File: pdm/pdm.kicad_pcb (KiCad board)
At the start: 2 copper layers, 169.5 x 69 mm, 112 parts, among them J1 Conn_01x04_Male, J2 Conn_01x08_Male, Q1 MMBT3904, Q10 Q_NPN_BCE, Q2 Q_NPN_BCE, Q3 MMBT3904, Q4 Q_NPN_BCE, Q5 MMBT3904, Q6 Q_NPN_BCE, Q7 MMBT3904, Q8 Q_NPN_BCE, Q9 MMBT3904, SW1 SW_Push, U1 AZ1117CH-3_3TRG1, U2 SN65HVD233, U3 STM32F042G6Ux, U4 BTS443P, U5 BTS443P, U6 BTS443P, U7 BTS443P, U8 BTS443P

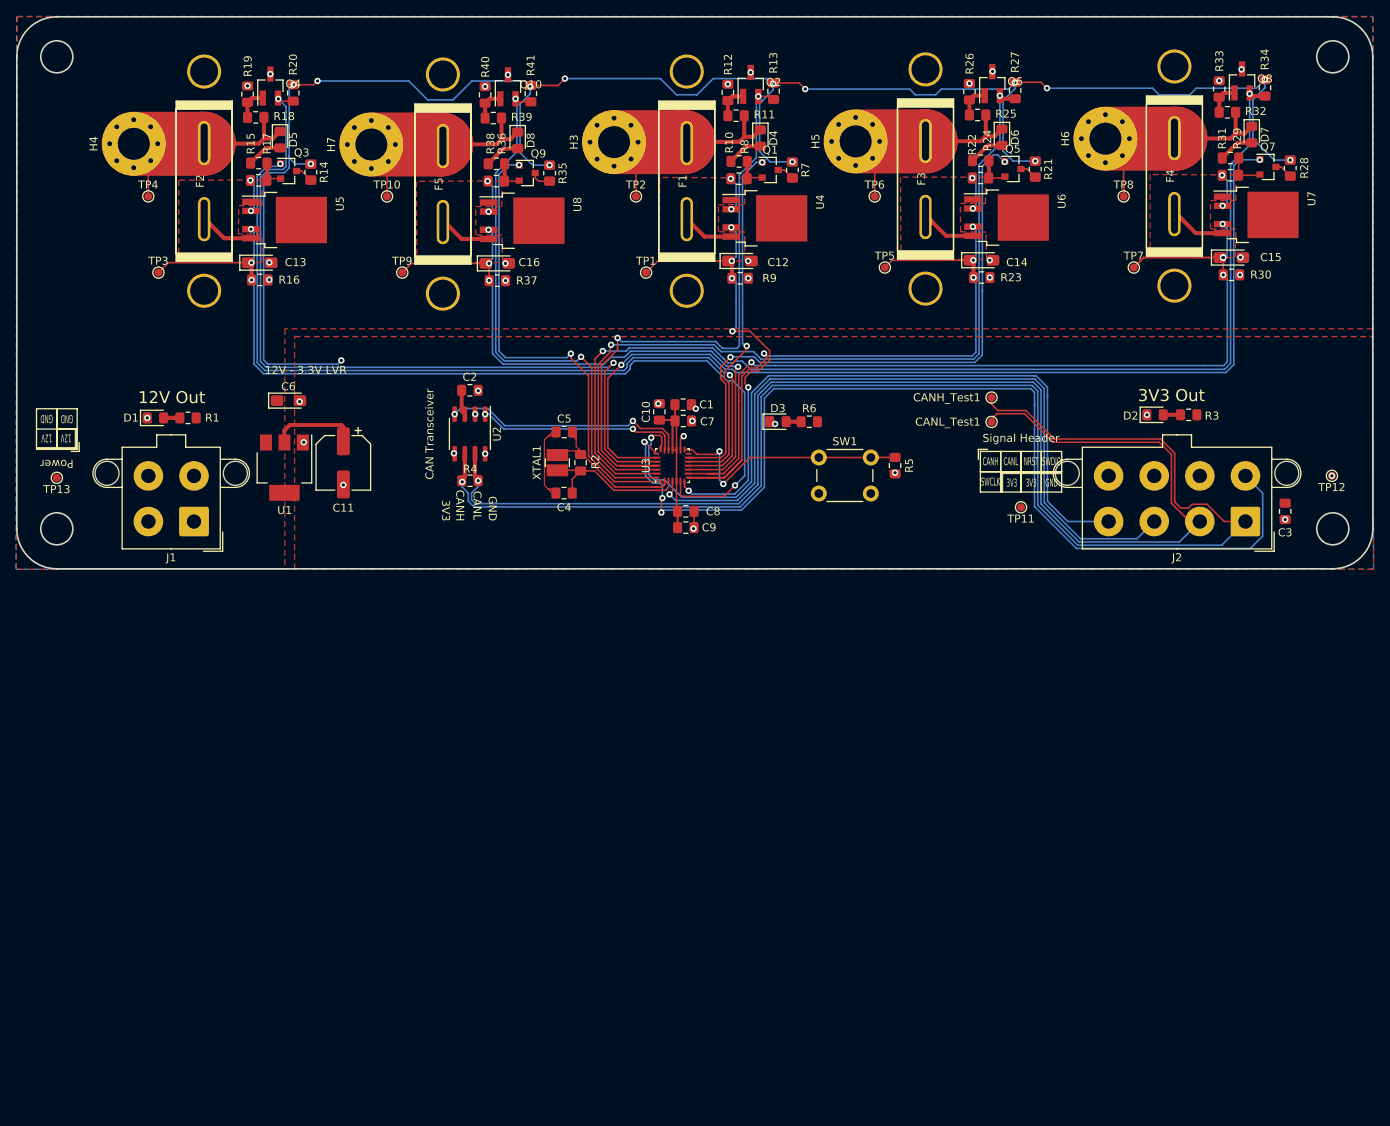
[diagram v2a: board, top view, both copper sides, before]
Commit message: changed layout with two plugs
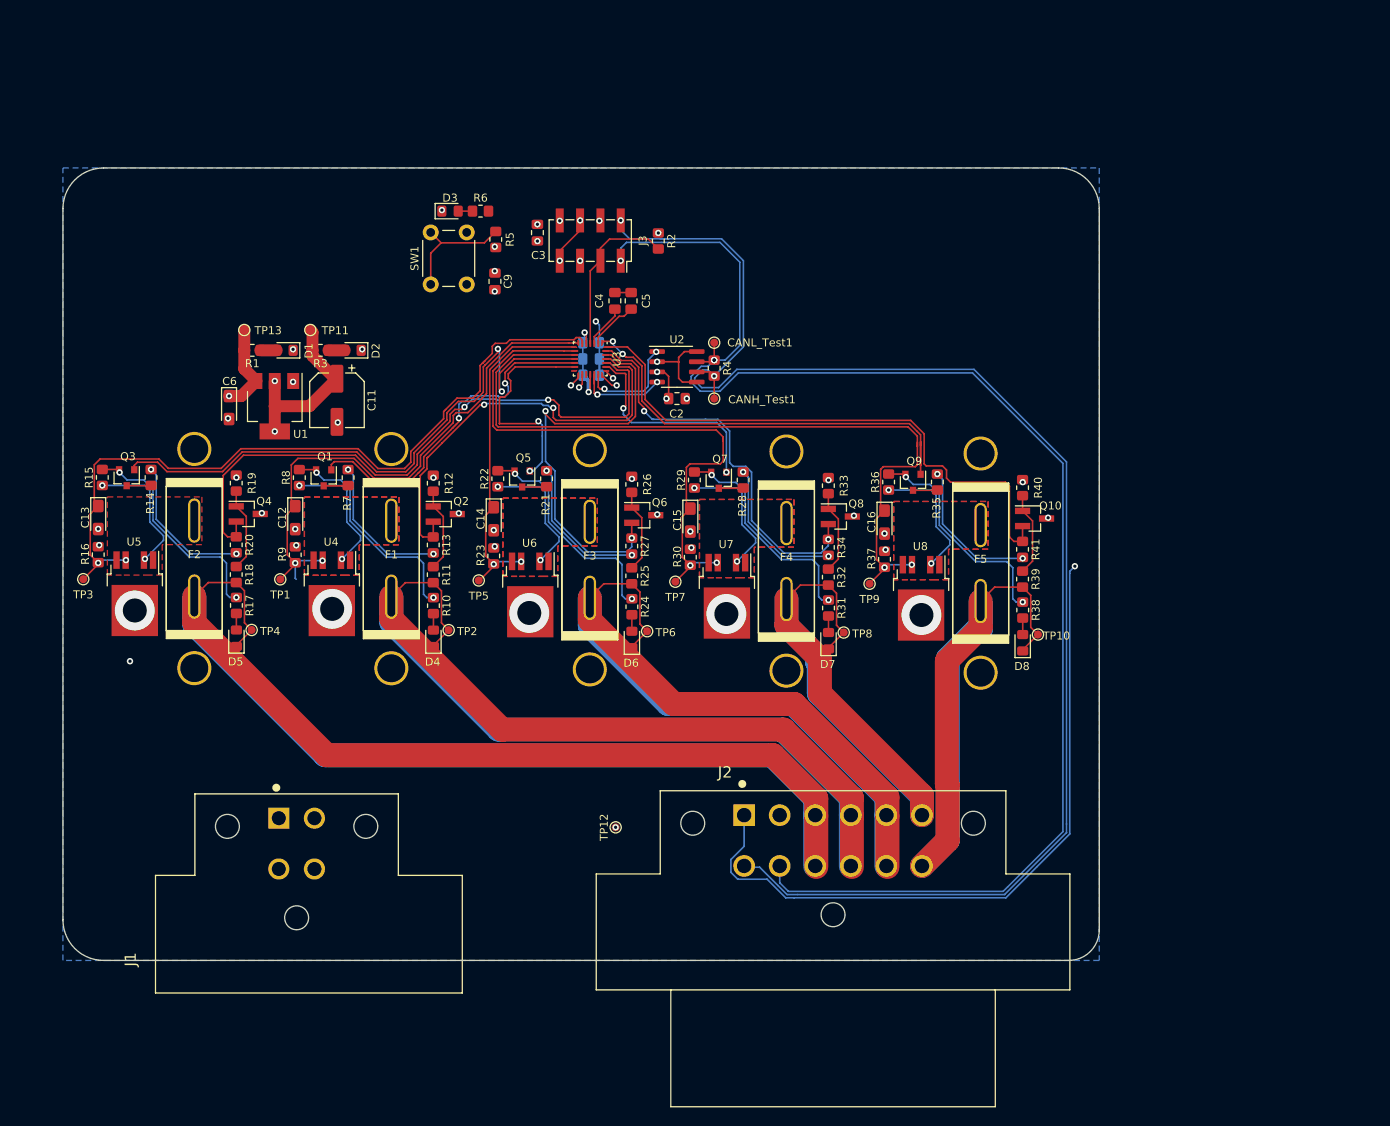
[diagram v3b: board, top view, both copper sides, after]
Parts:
- removed C1: 0.1uF, Capacitor_SMD:C_0805_2012Metric_Pad1.15x1.40mm_HandSolder
- removed H3, H4, H5, H6, H7: MountingHole_Pad, MountingHole:MountingHole_4mm_Pad_Via
- removed XTAL1: NX3225GD-8MHZ-STD-CRA-3, digikey-footprints:SMD-2_3.2x2.5mm
- added J3: Conn_01x08_Male, Connector_PinSocket_2.54mm:PinSocket_2x04_P2.54mm_Vertical_SMD, F.Cu at (170.2, 50.0)
- C10, C7, C8: footprint Capacitor_SMD:C_0805_2012Metric_Pad1.15x1.40mm_HandSolder -> Capacitor_SMD:C_0805_2012Metric_Pad1.18x1.45mm_HandSolder; moved to B.Cu
- C2, C3, C4, C5, C9: footprint Capacitor_SMD:C_0805_2012Metric_Pad1.15x1.40mm_HandSolder -> Capacitor_SMD:C_0805_2012Metric_Pad1.18x1.45mm_HandSolder
- F1, F2, F3, F4, F5: footprint Fuse:blade_fuse_panelized -> pdm_v2:fuseHolder
- J1: footprint Connector_Molex:Molex_Mega-Fit_76829-0004_2x02_P5.70mm_Vertical -> DT13-4P:TE_DT13-4P
- J2: value Conn_01x08_Male -> Conn_01x12_Male; footprint Connector_Molex:Molex_Mega-Fit_76829-0008_2x04_P5.70mm_Vertical -> DT13-12PB-B016:TE_DT13-12PB-B016
- R1, R10, R11, R12, R13, R15, R16, R17, R18, R19, R20, R22, R23, R24, R25, R26, R27, R29, R3, R30, R31, R32, R33, R34, R36, R37, R38, R39, R4, R40, R41, R5, R6, R8, R9: footprint Resistor_SMD:R_0805_2012Metric_Pad1.15x1.40mm_HandSolder -> Resistor_SMD:R_0805_2012Metric_Pad1.20x1.40mm_HandSolder
- R2: value 1M -> 10K; footprint Resistor_SMD:R_0805_2012Metric_Pad1.15x1.40mm_HandSolder -> Resistor_SMD:R_0805_2012Metric_Pad1.20x1.40mm_HandSolder
- moved R3 108.8 mm to (136.5, 63.7), turned to 180 degrees
- moved D2 100.6 mm to (140.5, 63.7), turned to 180 degrees
- moved C3 99.8 mm to (163.6, 49.0), turned to 90 degrees
- moved TP12 99.7 mm to (173.4, 123.3), turned to 90 degrees
- moved TP10 98.1 mm to (226.1, 99.2), turned to 180 degrees
- moved TP11 91.6 mm to (135.2, 61.2), turned to 270 degrees
- moved D8 89.0 mm to (224.2, 100.2), turned to 90 degrees
- moved R39 87.7 mm to (224.2, 92.3), turned to 270 degrees
- moved R38 86.3 mm to (224.2, 96.2), turned to 270 degrees
- moved Q10 85.1 mm to (225.7, 84.7), turned to 0 degrees
- moved R41 83.8 mm to (224.2, 88.6), turned to 270 degrees
- moved R40 83.2 mm to (224.2, 80.9)
- moved D7 82.5 mm to (200.0, 100.0), turned to 90 degrees
- moved F5 82.2 mm to (219.0, 90.3), turned to 180 degrees
- moved U7 81.6 mm to (187.3, 94.4), turned to 270 degrees
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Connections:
- net /fuse_block/vout renamed /fuse_block/out
- net /sheet5F955EDF/vout renamed /sheet5F955EDF/out
- net /sheet5F955F69/vout renamed /sheet5F955F69/out
- net /sheet5F95602F/vout renamed /sheet5F95602F/out
- net /sheet5F9560CD/vout renamed /sheet5F9560CD/out
- D4 pad 1: /sheet5F955EDF/vload -> /vout2
- D5 pad 1: /fuse_block/vload -> /vout1
- D6 pad 1: /sheet5F955F69/vload -> /vout3
- D7 pad 1: /sheet5F95602F/vload -> /vout4
- D8 pad 1: /sheet5F9560CD/vload -> /vout5
- F1 pad 1: /sheet5F955EDF/vload -> /vout2
- F2 pad 1: /fuse_block/vload -> /vout1
- F3 pad 1: /sheet5F955F69/vload -> /vout3
- F4 pad 1: /sheet5F95602F/vload -> /vout4
- F5 pad 1: /sheet5F9560CD/vload -> /vout5
- J1 pad 1: +12V -> GND
- J1 pad 3: GND -> +12V
- J1 pad 4: GND -> +12V
- J2 pad 1: /_P -> +3V3
- J2 pad 2: /_N -> GND
- J2 pad 3: /NRST -> /vout1
- J2 pad 4: /SWDIO -> /vout2
- J2 pad 5: /SWCLK -> /vout3
- J2 pad 6: +3V3 -> /vout4
- J2 pad 7: +3V3 -> /vout5
- J2 pad 8: GND -> /vout3
- R11 pad 2: /sheet5F955EDF/vload -> /vout2
- R18 pad 2: /fuse_block/vload -> /vout1
- R2 pad 1: /OSC_P -> GND
- R2 pad 2: /OSC_N -> /NRST
- R25 pad 2: /sheet5F955F69/vload -> /vout3
- R32 pad 2: /sheet5F95602F/vload -> /vout4
- R39 pad 2: /sheet5F9560CD/vload -> /vout5
- TP10 pad 1: /sheet5F9560CD/vload -> /vout5
- TP2 pad 1: /sheet5F955EDF/vload -> /vout2
- TP4 pad 1: /fuse_block/vload -> /vout1
- TP6 pad 1: /sheet5F955F69/vload -> /vout3
- TP8 pad 1: /sheet5F95602F/vload -> /vout4
- U1 pad 4: (no net) -> +3V3
- U3 pad 17: +3V3 -> (no net)
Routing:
- net /vout1: track 0.00 -> 311.6 mm
- net /vout2: track 0.00 -> 250.6 mm
- net /vout3: track 0.00 -> 189.4 mm
- net /vout5: track 0.00 -> 124.5 mm
- net /vout4: track 0.00 -> 117.8 mm
- net /SWCLK: track 127.0 -> 18.5 mm, vias 3 -> 2
- net /act4: track 124.8 -> 26.8 mm
- net /fuse4: track 138.5 -> 50.3 mm
- net /NRST: track 93.0 -> 20.7 mm, vias 1 -> 0
- net /SWDIO: track 95.6 -> 24.5 mm, vias 1 -> 2
- net +12V: track 0.00 -> 57.6 mm, vias 0 -> 7
- net /fuse3: track 104.7 -> 51.7 mm
- net /act3: track 78.5 -> 28.2 mm
- net +3V3: track 270.4 -> 226.4 mm, vias 15 -> 21
- net /sense3: track 84.7 -> 43.5 mm, vias 4 -> 2
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- added copper zone on In2.Cu, net +12V
- added copper zone on In1.Cu, net +3V3
- removed copper zone on F.Cu, net +12V
- removed copper zone on F.Cu, net +3V3
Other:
- board size 169.5 x 69 mm -> 129.5 x 99.1 mm
- copper layers 2 -> 4
- board text removed: "12V"
- board text removed: "12V - 3.3V LVR"
- board text removed: "12V Out"
- board text removed: "3V3"
- board text removed: "3V3 Out"
- board text removed: "CAN Transceiver"
- board text removed: "CANH"
- board text removed: "CANL"
- board text removed: "GND"
- board text removed: "NRST"
- board text removed: "Power"
- board text removed: "SWCLK"
- board text removed: "SWDIO"
- board text removed: "Signal Header"

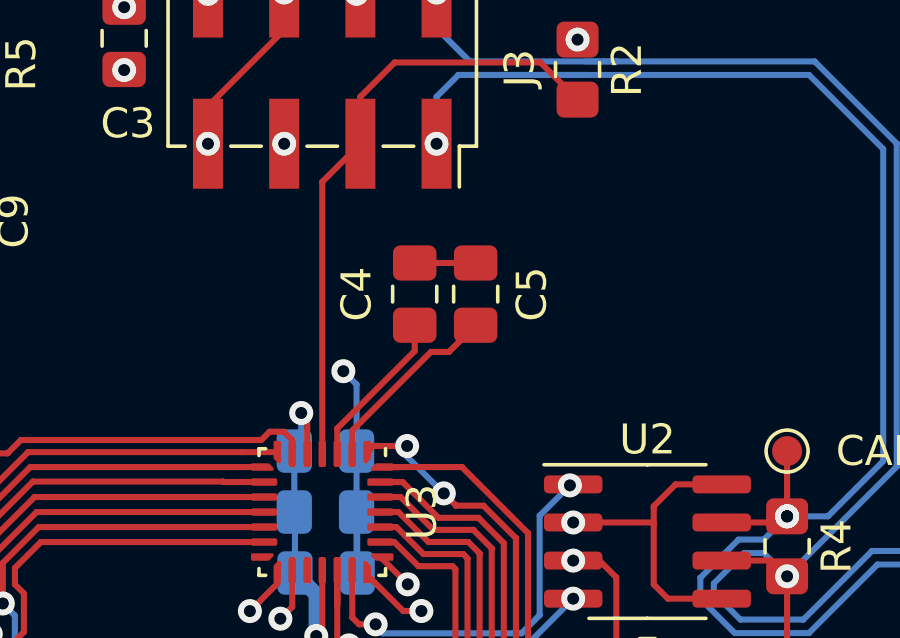
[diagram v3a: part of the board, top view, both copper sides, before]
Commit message: added placeholder oscillator
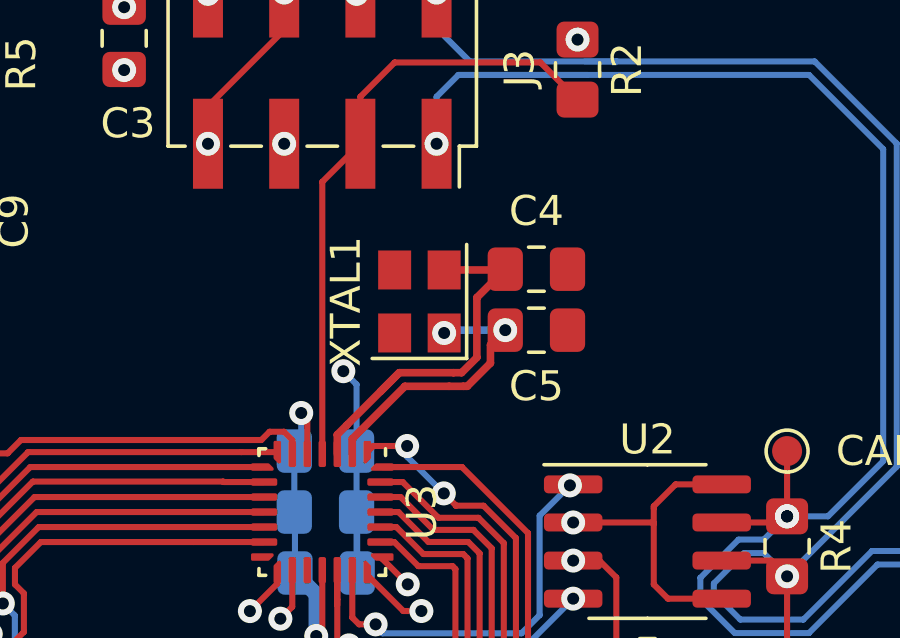
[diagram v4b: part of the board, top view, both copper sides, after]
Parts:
- added XTAL1: NX3225GD-8MHZ-STD-CRA-3, Oscillator:Oscillator_SMD_Abracon_ASE-4Pin_3.2x2.5mm, F.Cu at (173.4, 57.8)
- moved C4 4.14 mm to (177.3, 56.7), turned to 180 degrees
- moved C5 2.35 mm to (177.3, 58.7), turned to 180 degrees
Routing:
- net /OSC_P: track 5.36 -> 12.6 mm
- net /OSC_N: track 6.35 -> 9.53 mm, vias 0 -> 2
- net Net-(C4-Pad1): track 2.03 -> 0.00 mm

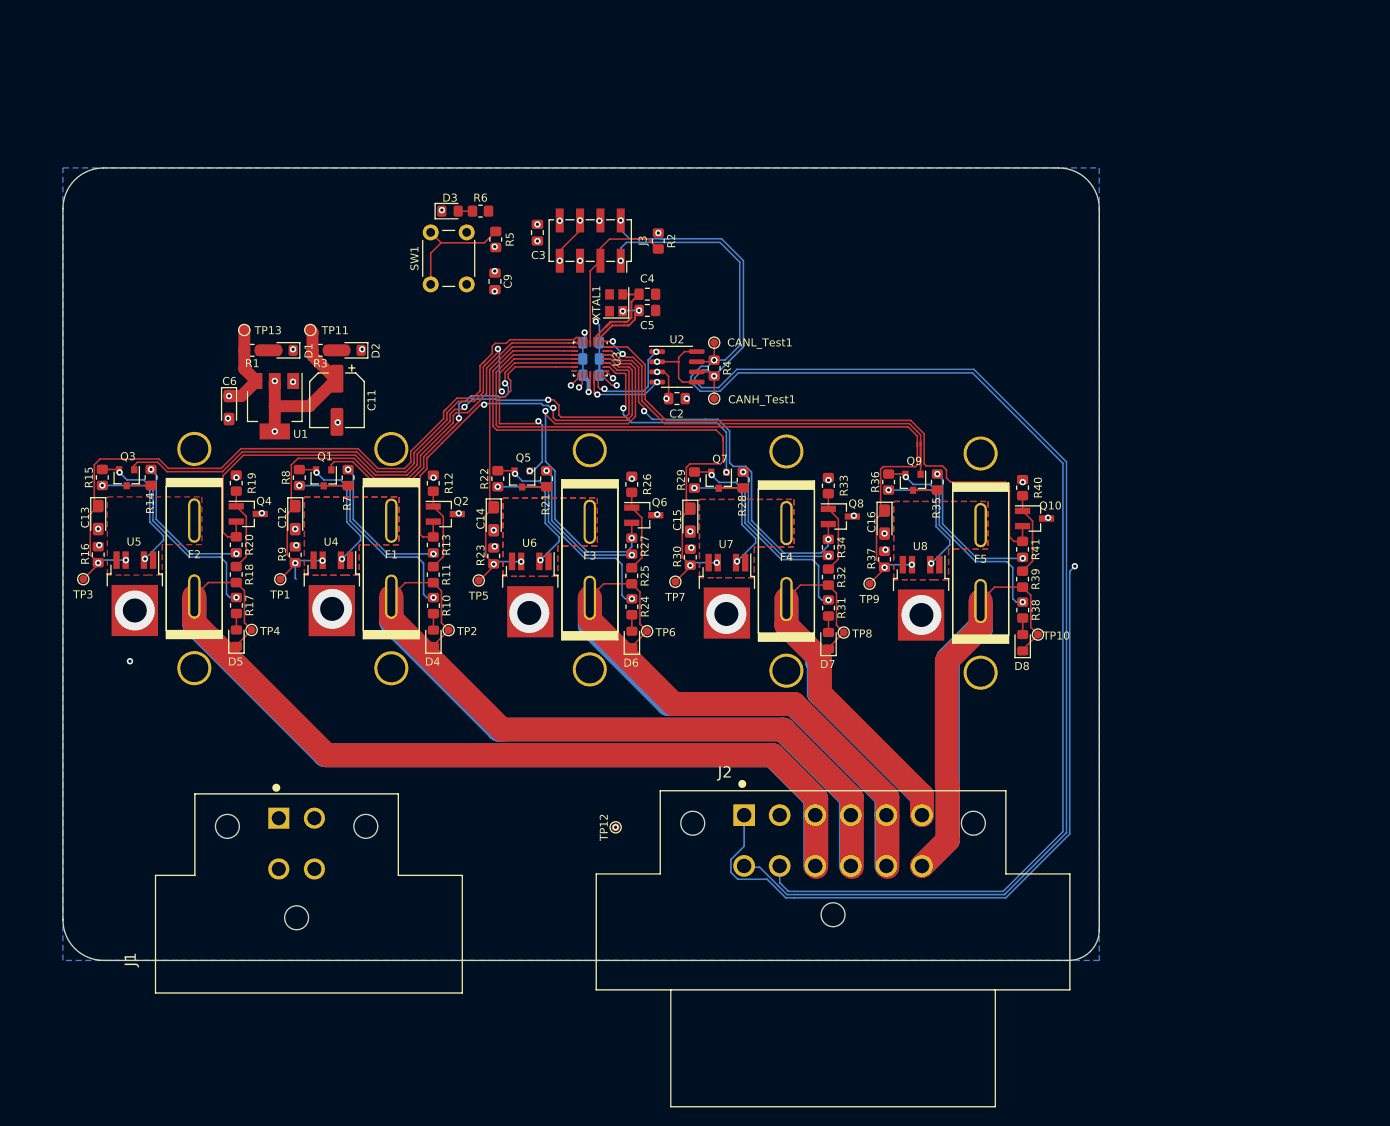
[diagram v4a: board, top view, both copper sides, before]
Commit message: added mount and moved 12 pin
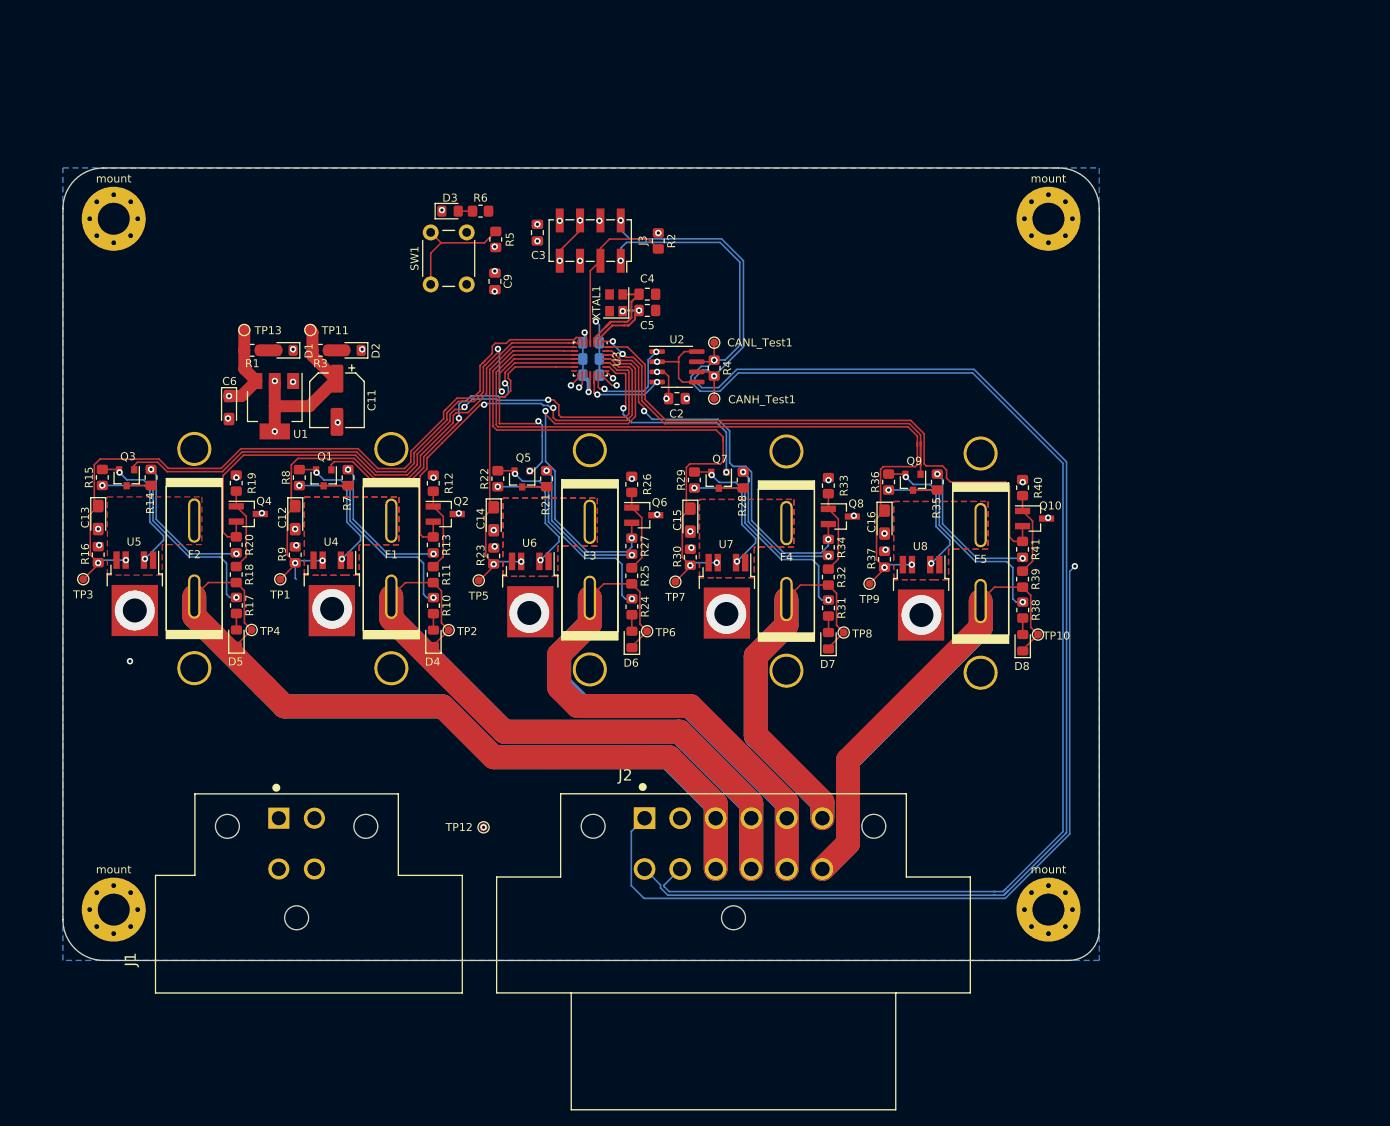
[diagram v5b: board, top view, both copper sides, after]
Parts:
- added mount: MountingHole_4mm_Pad_Via, MountingHole:MountingHole_4mm_Pad_Via, F.Cu at (227.5, 133.6)
- added mount: MountingHole_4mm_Pad_Via, MountingHole:MountingHole_4mm_Pad_Via, F.Cu at (110.6, 133.6)
- added mount: MountingHole_4mm_Pad_Via, MountingHole:MountingHole_4mm_Pad_Via, F.Cu at (227.5, 47.2)
- added mount: MountingHole_4mm_Pad_Via, MountingHole:MountingHole_4mm_Pad_Via, F.Cu at (110.6, 47.2)
- moved TP12 16.5 mm to (156.8, 123.3)
- moved J2 12.5 mm to (188.1, 128.5)
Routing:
- net /vout1: track 311.6 -> 272.3 mm
- net /vout2: track 250.6 -> 212.2 mm
- net /vout5: track 124.5 -> 140.8 mm
- net /_N: track 181.1 -> 196.9 mm
- net /_P: track 187.8 -> 201.1 mm
- net +3V3: track 226.4 -> 239.5 mm
- net /vout3: track 189.4 -> 181.9 mm
- net /vout4: track 117.8 -> 113.0 mm
